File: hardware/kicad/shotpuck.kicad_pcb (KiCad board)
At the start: 2 copper layers, 36 x 34.8 mm, 31 parts, among them J1 Samzo PR5L4015-2P-C-F, J2 SWD pads, Q1 DMN63D8LDW, Q2 DMN2004DWK, U1 MDBT50Q-1MV2, U2 LSM6DSO32TR, U3 MCP73831T-2ACI/OT, U4 BQ29700DSER

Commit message: Enhance ShotPuck design with mechanical and layout improvements
- Updated mechanical design in `puck.py` to include a stepped connector for improved fit and stability.
- Revised `layout.json` to reflect new connector dimensions and added detailed descriptions for clarity.
- Enhanced assembly instructions in `README.md` to specify RTV sealing around the connector.
- Improved validation steps in `VALIDATION.md` to ensure reliable magnetic plug engagement and seal integrity.
- Added new parameters in `geometry.py` for lip wall and gap to support design adjustments.

Co-Authored-By: Claude Opus 5.5 <noreply@anthropic.com>
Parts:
- turned J2 to 0 degrees
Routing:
- net VIN: track 21.6 -> 10.1 mm
- net GND: track 24.6 -> 23.4 mm, vias 22 -> 21

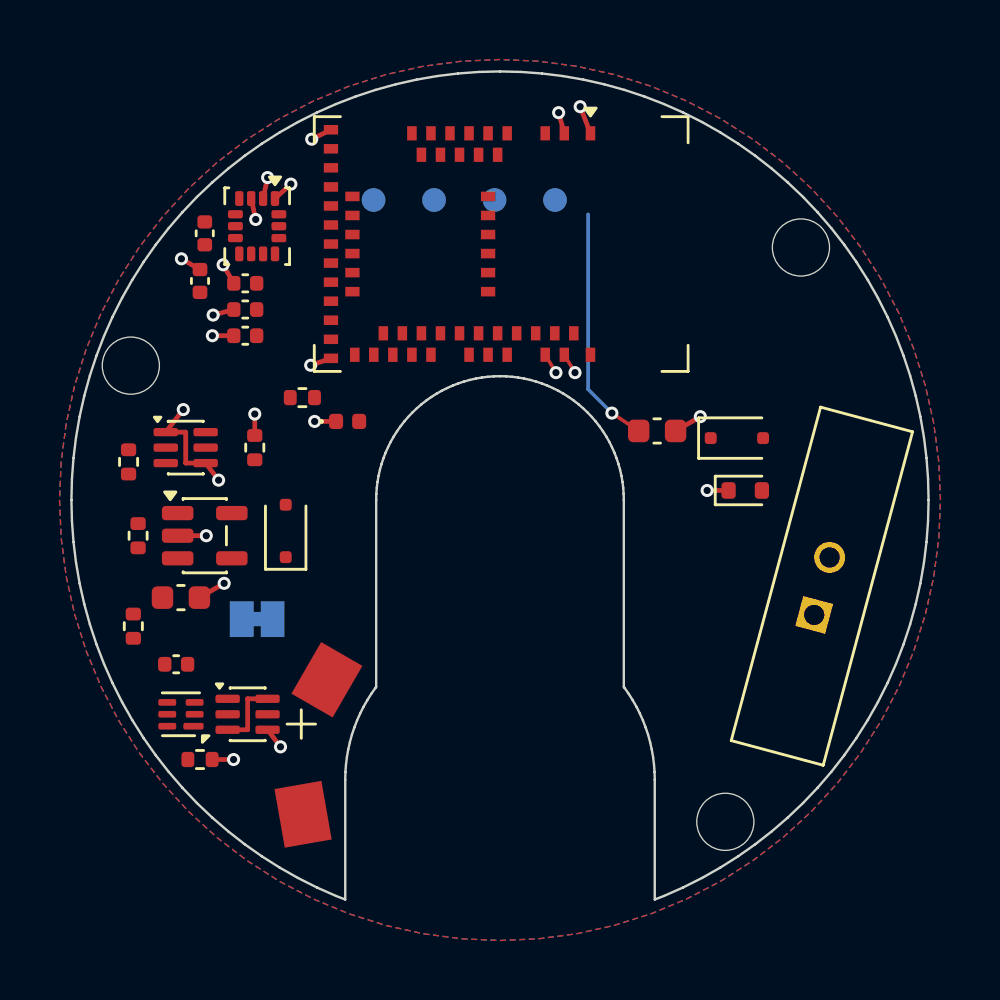
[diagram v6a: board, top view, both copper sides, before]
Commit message: Refine ShotPuck design and documentation for improved functionality and clarity
- Updated `HANDOVER.md` to clarify PCB routing and placement procedures, emphasizing the importance of running `gen_pcb.py --no-route` and `global_route.py` for optimal results.
- Revised `README.md` to correct the center of mass measurement and enhance the description of the puck's dimensions.
- Enhanced `VALIDATION.md` to reflect updated weight and balance metrics, ensuring accurate representation of the ShotPuck's specifications.
- Adjusted `design.py` to include new charge-input protection details and updated component specifications for better clarity.
- Improved `gen_bom.py` and `gen_jlc.py` to reflect changes in component sourcing and specifications.

Co-Authored-By: Claude Opus 5.5 <noreply@anthropic.com>
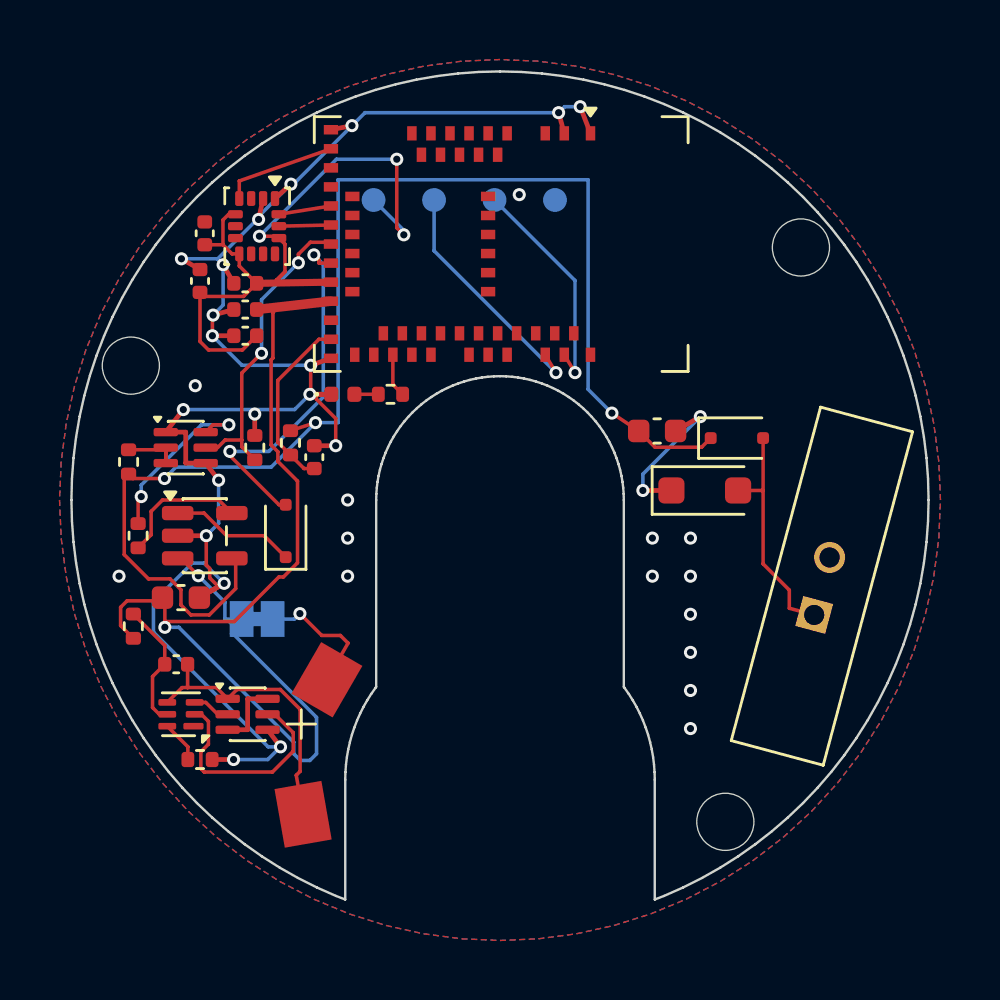
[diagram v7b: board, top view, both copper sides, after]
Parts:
- added C9: 100n, Capacitor_SMD:C_0402_1005Metric, F.Cu at (-7.80, -1.80)
- added R9: 1k, Resistor_SMD:R_0402_1005Metric, F.Cu at (-8.80, -2.40)
- C2: value 4.7u 10V -> 10u 10V
- D3: value PESD5V0S1BB -> SMF5.0CA; footprint Diode_SMD:D_SOD-523 -> Diode_SMD:D_SOD-123F
- D4: value LED green 0402 -> LED yellow-green 0402
- moved R4 3.70 mm to (-4.60, -4.44), turned to 180 degrees
- moved D3 1.70 mm to (8.60, -0.40)
- moved D4 1.16 mm to (-6.60, -4.44)
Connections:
- U1 pad 16: CHG_INH -> ACC_INT1
- U1 pad 24: ACC_INT1 -> CHG_INH
- U1 pad 32: VIN -> VBUS_SNS
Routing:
- net GND: track 23.4 -> 86.8 mm, vias 21 -> 35
- net VIN: track 10.1 -> 58.1 mm, vias 1 -> 3
- net VBAT: track 0.00 -> 46.7 mm, vias 0 -> 2
- net VDD: track 0.00 -> 31.7 mm, vias 0 -> 3
- net CHG_STAT: track 0.00 -> 15.3 mm, vias 0 -> 2
- net CHG_INH: track 0.00 -> 13.1 mm, vias 0 -> 2
- net BAT_N: track 0.00 -> 12.0 mm
- net VIN_RAW: track 0.00 -> 9.74 mm
- net SWDIO: track 0.87 -> 10.2 mm
- net PCM_COUT: track 0.00 -> 9.30 mm
- net SWDCLK: track 0.87 -> 9.52 mm
- net VBUS_SNS: track 0.00 -> 7.54 mm
- net PROG_SW: track 0.00 -> 7.51 mm, vias 0 -> 2
- net PROG: track 0.00 -> 5.57 mm
- net BAT_P: track 0.00 -> 5.55 mm, vias 0 -> 1
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
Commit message: Update ShotPuck design to integrate u-blox BMD-340 module and enhance documentation
- Replaced the Raytac MDBT50Q-1MV2 with the u-blox BMD-340-A-R-10 in the hardware design, updating relevant specifications in `HANDOVER.md`, `README.md`, and `VALIDATION.md`.
- Adjusted pin mappings and configurations in firmware files to reflect the new module's layout and capabilities.
- Enhanced `layout.json` and `design.py` to accommodate the new component dimensions and positions.
- Updated the bill of materials and JLCPCB configurations in `gen_bom.py` and `gen_jlc.py` to ensure accurate sourcing of the new module.
- Revised mechanical design parameters in `board_shape.py` to improve fit and stability.

Co-Authored-By: Claude Opus 5.5 <noreply@anthropic.com>
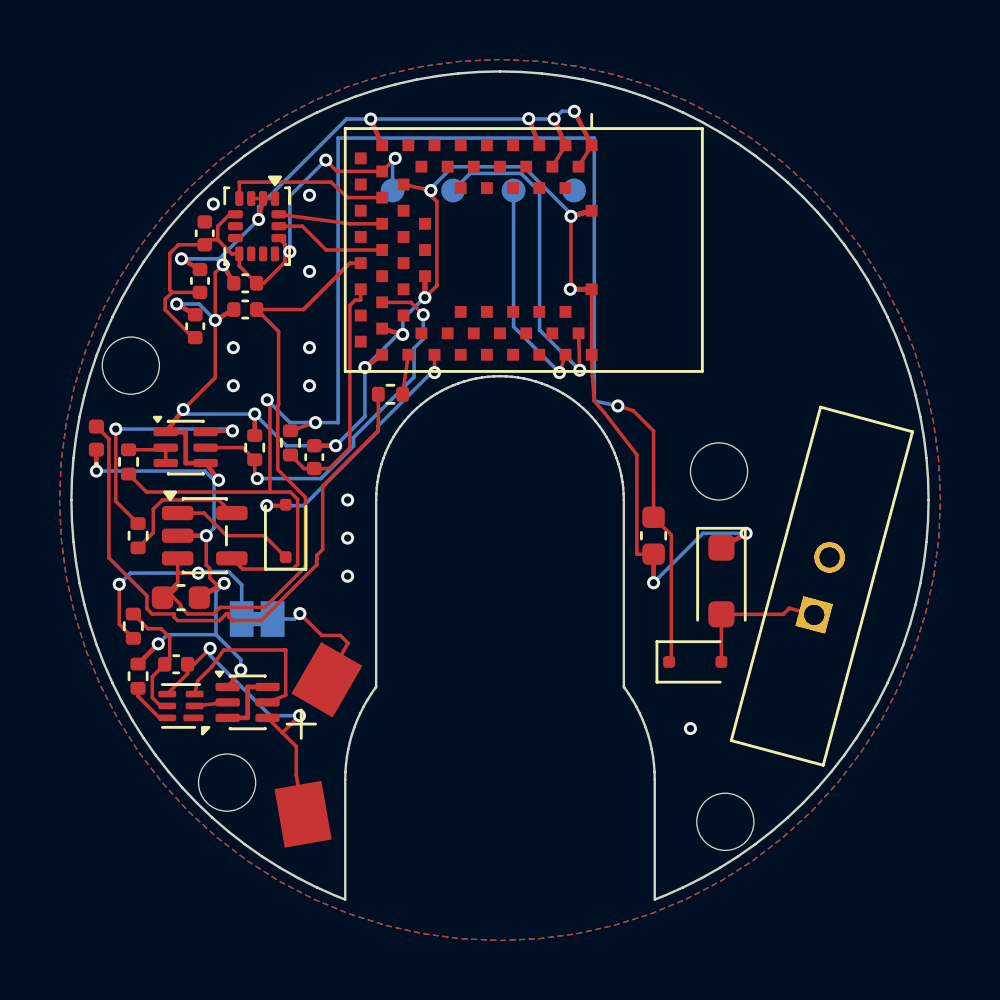
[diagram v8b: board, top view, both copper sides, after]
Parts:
- added H4: M2, ShotPuck:MountingHole_2.4mm_NPTH, F.Cu at (-11.5, 11.9)
- U1: value MDBT50Q-1MV2 -> BMD-340-A-R; footprint RF_Module:Raytac_MDBT50Q -> ShotPuck:u-blox_BMD-340
- moved D4 10.5 mm to (-16.9, -2.60), turned to 90 degrees
- moved H1 10.0 mm to (9.20, -1.20)
- moved D1 9.56 mm to (8.20, 6.80)
- moved C1 4.40 mm to (6.45, 1.50), turned to -90 degrees
- moved R8 4.36 mm to (-15.2, 7.40), turned to 90 degrees
- moved D3 3.86 mm to (9.30, 3.40), turned to -90 degrees
- moved C4 2.77 mm to (-12.8, -7.30), turned to 90 degrees
- moved C5 2.20 mm to (-10.7, -9.10)
- moved U1 0.98 mm to (1.00, -10.5), turned to 180 degrees
- moved J2 0.89 mm to (-0.70, -13.0)
- moved Q2 0.50 mm to (-10.6, 8.50)
- moved U4 0.35 mm to (-13.4, 8.65)
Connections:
- Q2 pad 1: BAT_N -> GND
- Q2 pad 2: PCM_DOUT -> PCM_COUT
- Q2 pad 4: GND -> BAT_N
- Q2 pad 5: PCM_COUT -> PCM_DOUT
- U1 pad 15: GND -> (no net)
- U1 pad 16: ACC_INT1 -> GND
- U1 pad 17: (no net) -> VDD
- U1 pad 18: (no net) -> GND
- U1 pad 19: (no net) -> ACC_INT1
- U1 pad 20: SDA -> (no net)
- U1 pad 21: (no net) -> SDA
- U1 pad 22: SCL -> (no net)
- U1 pad 23: (no net) -> SCL
- U1 pad 24: CHG_INH -> (no net)
- U1 pad 26: CHG_STAT -> (no net)
- U1 pad 27: (no net) -> CHG_INH
- U1 pad 28: VDD -> (no net)
- U1 pad 29: (no net) -> GND
- U1 pad 3: (no net) -> GND
- U1 pad 30: VBAT -> GND
- U1 pad 31: (no net) -> LED_IO
- U1 pad 32: VBUS_SNS -> (no net)
- U1 pad 33: GND -> CHG_STAT
- U1 pad 37: LED_IO -> (no net)
- U1 pad 4: (no net) -> GND
- U1 pad 43: (no net) -> SWDCLK
- U1 pad 44: (no net) -> SWDIO
- U1 pad 45: (no net) -> GND
- U1 pad 46: (no net) -> GND
- U1 pad 47: (no net) -> GND
- U1 pad 5: (no net) -> GND
- U1 pad 51: SWDIO -> (no net)
- U1 pad 53: SWDCLK -> (no net)
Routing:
- net GND: track 86.8 -> 131.6 mm, vias 35 -> 37
- net LED_A: track 1.00 -> 25.4 mm
- net VIN: track 58.1 -> 68.4 mm
- net PCM_COUT: track 9.30 -> 1.40 mm
- net VDD: track 31.7 -> 24.0 mm
- net VBAT: track 46.7 -> 39.4 mm
- net PCM_DOUT: track 1.59 -> 7.59 mm
- net PROG_SW: track 7.51 -> 11.5 mm
- net SWDIO: track 10.2 -> 14.0 mm
- net VIN_RAW: track 9.74 -> 6.04 mm
- net CHG_STAT: track 15.3 -> 11.8 mm
- net CHG_INH: track 13.1 -> 16.4 mm
- net SCL: track 2.19 -> 4.75 mm
- net VBUS_SNS: track 7.54 -> 10.1 mm
- net SDA: track 2.22 -> 4.36 mm
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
